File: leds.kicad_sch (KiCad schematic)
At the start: 20 parts

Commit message: Updated layout and schem
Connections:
- net 12v_PWD_LED_VOL_DIV: now reaches R6.1, R7.1, R8.1
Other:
- moved on the sheet: R7
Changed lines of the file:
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@@
+	)
+	(junction
+		(at 208.28 41.91)
+		(diameter 0)
+		(color 0 0 0 0)
 	)
 	(junction
@@
 	(wire
 		(pts
+			(xy 208.28 41.91) (xy 212.09 41.91)
+		)
+		(stroke
+			(width 0)
+			(type default)
+		)
+	)
+	(wire
+		(pts
 			(xy 173.99 38.1) (xy 181.61 38.1)
 		)
@@
 	(wire
 		(pts
-			(xy 208.28 41.91) (xy 208.28 38.1)
+			(xy 208.28 43.18) (xy 208.28 41.91)
 		)
 		(stroke
@@
 	(wire
 		(pts
-			(xy 208.28 49.53) (xy 208.28 50.8)
+			(xy 208.28 50.8) (xy 208.28 53.34)
 		)
 		(stroke
@@
 		(pts
 			(xy 129.54 35.56) (xy 129.54 46.99)
+		)
+		(stroke
+			(width 0)
+			(type default)
+		)
+	)
+	(wire
+		(pts
+			(xy 208.28 38.1) (xy 208.28 41.91)
 		)
 		(stroke
@@
 	(label "PUMP_PWM_IND_LED_5v"
 		(at 52.07 66.04 0)
+		(fields_autoplaced yes)
+		(effects
+			(font
+				(size 1.27 1.27)
+			)
+			(justify left bottom)
+		)
+	)
+	(label "12v_PWD_LED_VOL_DIV"
+		(at 212.09 41.91 0)
 		(fields_autoplaced yes)
 		(effects
@@
 	(symbol
 		(lib_id "Device:R")
-		(at 208.28 45.72 0)
+		(at 208.28 46.99 0)
 		(unit 1)
 		(exclude_from_sim no)
@@
 		(fields_autoplaced yes)
 		(property "Reference" "R7"
-			(at 210.82 44.4499 0)
+			(at 210.82 45.7199 0)
 			(effects
 				(font
@@
 		)
 		(property "Value" "470R"
-			(at 210.82 46.9899 0)
+			(at 210.82 48.2599 0)
 			(effects
 				(font
@@
 		)
 		(property "Footprint" "Resistor_SMD:R_0805_2012Metric"
-			(at 206.502 45.72 90)
+			(at 206.502 46.99 90)
 			(effects
 				(font
@@
 		)
 		(property "Datasheet" "~"
-			(at 208.28 45.72 0)
+			(at 208.28 46.99 0)
 			(effects
 				(font
@@
 		)
 		(property "Description" "Resistor"
-			(at 208.28 45.72 0)
+			(at 208.28 46.99 0)
 			(effects
 				(font
@@
 	(symbol
 		(lib_id "power:GND")
-		(at 208.28 50.8 0)
+		(at 208.28 53.34 0)
 		(unit 1)
 		(exclude_from_sim no)
@@
 		(fields_autoplaced yes)
 		(property "Reference" "#PWR049"
-			(at 208.28 57.15 0)
+			(at 208.28 59.69 0)
 			(effects
 				(font
@@
 		)
 		(property "Value" "GND"
-			(at 208.28 55.88 0)
+			(at 208.28 58.42 0)
 			(effects
 				(font
@@
 		)
 		(property "Footprint" ""
-			(at 208.28 50.8 0)
+			(at 208.28 53.34 0)
 			(effects
 				(font
@@
 		)
 		(property "Datasheet" ""
-			(at 208.28 50.8 0)
+			(at 208.28 53.34 0)
 			(effects
 				(font
@@
 		)
 		(property "Description" "Power symbol creates a global label with name \"GND\" , ground"
-			(at 208.28 50.8 0)
-			(effects
-				(font
+			(at 208.28 53.34 0)
+			(effects
+				(font

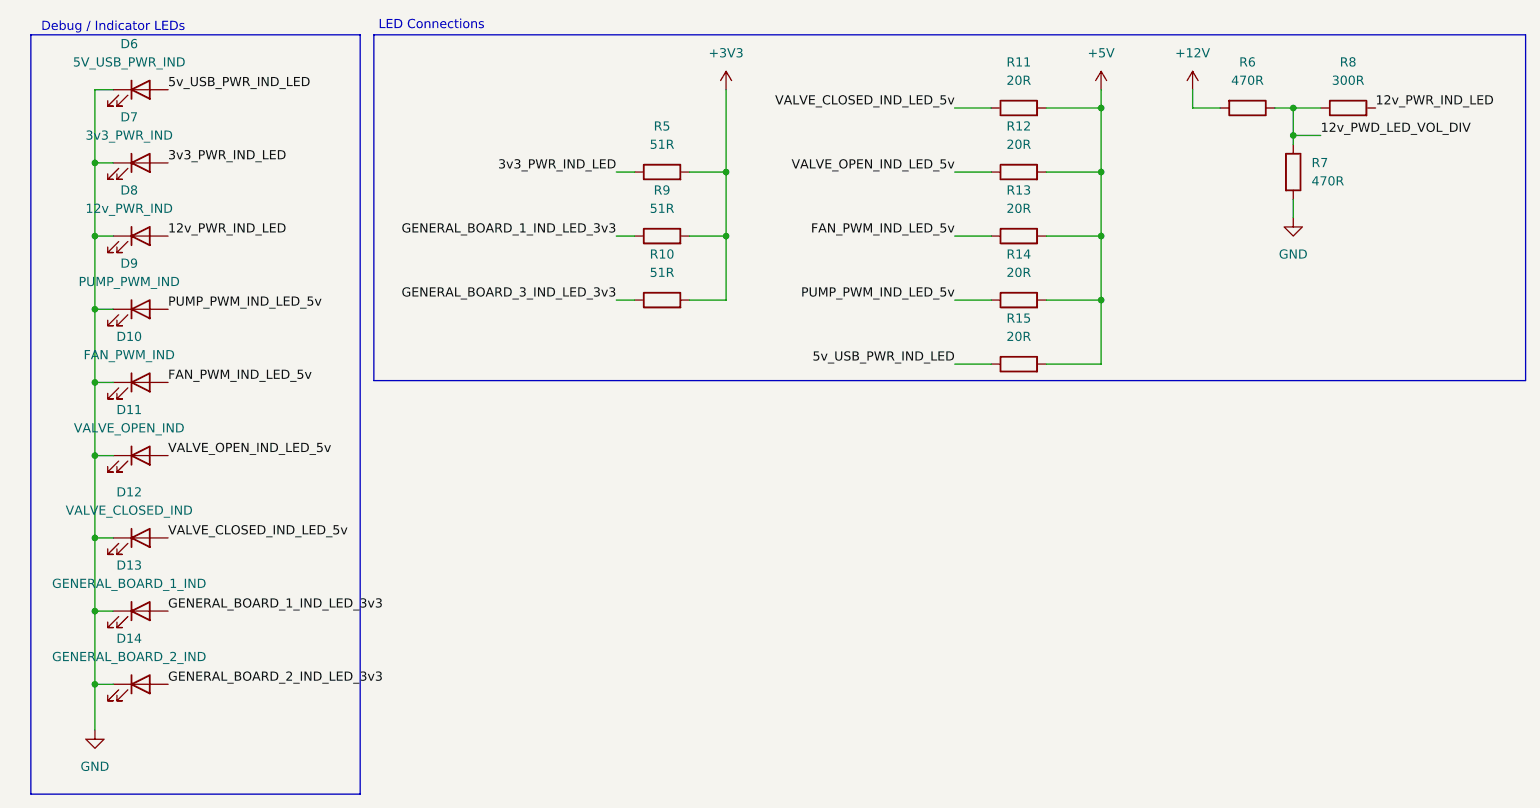
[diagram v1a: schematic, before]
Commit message: Layout of indicator LEDs. Shrank design space
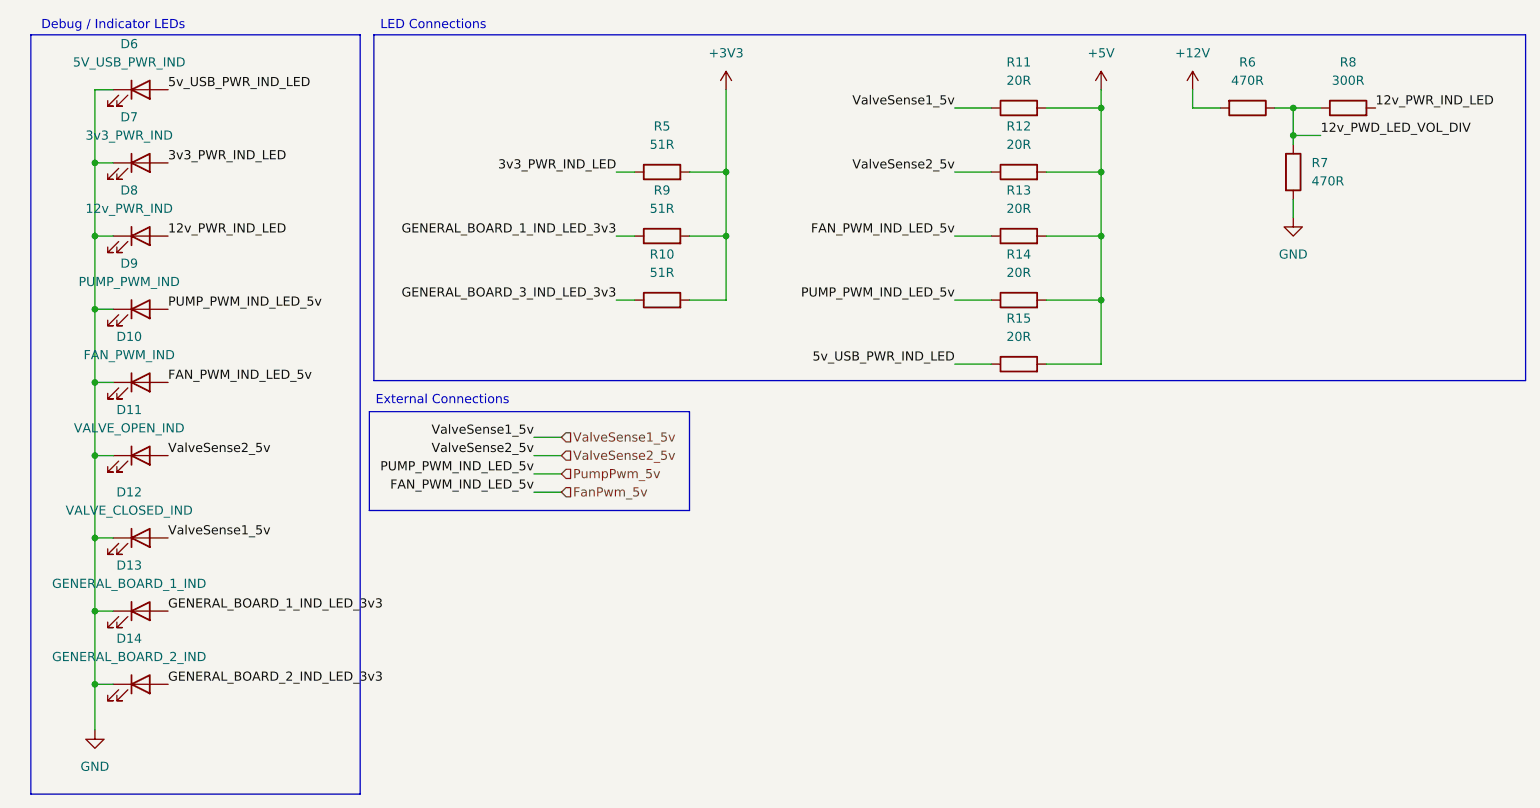
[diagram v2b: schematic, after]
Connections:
- net FAN_PWM_IND_LED_5v renamed FanPwm_5v
- net PUMP_PWM_IND_LED_5v renamed PumpPwm_5v
- net VALVE_CLOSED_IND_LED_5v renamed ValveSense1_5v
- net VALVE_OPEN_IND_LED_5v renamed ValveSense2_5v
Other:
- note added: "External Connections"
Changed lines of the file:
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@@
+	(wire
+		(pts
+			(xy 102.87 86.36) (xy 106.68 86.36)
+		)
+		(stroke
+			(width 0)
+			(type default)
+		)
+	)
 	(wire
 		(pts
@@
 	(wire
 		(pts
+			(xy 102.87 83.82) (xy 106.68 83.82)
+		)
+		(stroke
+			(width 0)
+			(type default)
+		)
+	)
+	(wire
+		(pts
 			(xy 114.3 55.88) (xy 116.84 55.88)
 		)
@@
 	(wire
 		(pts
+			(xy 102.87 91.44) (xy 106.68 91.44)
+		)
+		(stroke
+			(width 0)
+			(type default)
+		)
+	)
+	(wire
+		(pts
 			(xy 129.54 46.99) (xy 124.46 46.99)
 		)
@@
 		(pts
 			(xy 41.91 118.11) (xy 41.91 107.95)
+		)
+		(stroke
+			(width 0)
+			(type default)
+		)
+	)
+	(wire
+		(pts
+			(xy 102.87 88.9) (xy 106.68 88.9)
 		)
 		(stroke
@@
 		)
 	)
+	(rectangle
+		(start 80.01 80.264)
+		(end 124.46 93.98)
+		(stroke
+			(width 0)
+			(type default)
+		)
+		(fill
+			(type none)
+		)
+	)
 	(text "Debug / Indicator LEDs"
 		(exclude_from_sim no)
-		(at 44.45 26.924 0)
+		(at 44.45 26.67 0)
+		(effects
+			(font
+				(size 1.27 1.27)
+			)
+		)
+	)
+	(text "External Connections"
+		(exclude_from_sim no)
+		(at 90.17 78.74 0)
 		(effects
 			(font
@@
 	(text "LED Connections"
 		(exclude_from_sim no)
-		(at 88.646 26.67 0)
+		(at 88.9 26.67 0)
 		(effects
 			(font
@@
 		)
 	)
+	(label "ValveSense2_5v"
+		(at 52.07 86.36 0)
+		(fields_autoplaced yes)
+		(effects
+			(font
+				(size 1.27 1.27)
+			)
+			(justify left bottom)
+		)
+	)
+	(label "FAN_PWM_IND_LED_5v"
+		(at 102.87 91.44 180)
+		(fields_autoplaced yes)
+		(effects
+			(font
+				(size 1.27 1.27)
+			)
+			(justify right bottom)
+		)
+	)
 	(label "FAN_PWM_IND_LED_5v"
 		(at 52.07 76.2 0)
@@
 		)
 	)
+	(label "PUMP_PWM_IND_LED_5v"
+		(at 102.87 88.9 180)
+		(fields_autoplaced yes)
+		(effects
+			(font
+				(size 1.27 1.27)
+			)
+			(justify right bottom)
+		)
+	)
 	(label "5v_USB_PWR_IND_LED"
 		(at 52.07 35.56 0)
@@
 		)
 	)
+	(label "ValveSense1_5v"
+		(at 102.87 83.82 180)
+		(fields_autoplaced yes)
+		(effects
+			(font
+				(size 1.27 1.27)
+			)
+			(justify right bottom)
+		)
+	)
 	(label "GENERAL_BOARD_1_IND_LED_3v3"
 		(at 114.3 55.88 180)
@@
 		)
 	)
+	(label "ValveSense1_5v"
+		(at 52.07 97.79 0)
+		(fields_autoplaced yes)
+		(effects
+			(font
+				(size 1.27 1.27)
+			)
+			(justify left bottom)
+		)
+	)
 	(label "3v3_PWR_IND_LED"
 		(at 52.07 45.72 0)
@@
 		)
 	)
-	(label "VALVE_CLOSED_IND_LED_5v"
-		(at 52.07 97.79 0)
-		(fields_autoplaced yes)
-		(effects
-			(font
-				(size 1.27 1.27)
-			)
-			(justify left bottom)
-		)
-	)
-	(label "VALVE_OPEN_IND_LED_5v"
+	(label "ValveSense2_5v"
 		(at 161.29 46.99 180)
 		(fields_autoplaced yes)
@@
 		)
 	)
+	(label "ValveSense2_5v"
+		(at 102.87 86.36 180)
+		(fields_autoplaced yes)
+		(effects
+			(font
+				(size 1.27 1.27)
+			)
+			(justify right bottom)
+		)
+	)
+	(label "ValveSense1_5v"
+		(at 161.29 38.1 180)
+		(fields_autoplaced yes)
+		(effects
+			(font
+				(size 1.27 1.27)
+			)
+			(justify right bottom)
+		)
+	)
 	(label "GENERAL_BOARD_3_IND_LED_3v3"
 		(at 114.3 64.77 180)
@@
 		)
 	)
-	(label "VALVE_CLOSED_IND_LED_5v"
-		(at 161.29 38.1 180)
-		(fields_autoplaced yes)
-		(effects
-			(font
-				(size 1.27 1.27)
-			)
-			(justify right bottom)
-		)
-	)
-	(label "VALVE_OPEN_IND_LED_5v"
-		(at 52.07 86.36 0)
-		(fields_autoplaced yes)
-		(effects
-			(font
-				(size 1.27 1.27)
-			)
-			(justify left bottom)
-		)
-	)
+	(hierarchical_label "ValveSense2_5v"
+		(shape input)
+		(at 106.68 86.36 0)
+		(fields_autoplaced yes)
+		(effects
+			(font
+				(size 1.27 1.27)
+			)
+			(justify left)
+		)
+	)
+	(hierarchical_label "PumpPwm_5v"
+		(shape input)
+		(at 106.68 88.9 0)
+		(fields_autoplaced yes)
+		(effects
+			(font
+				(size 1.27 1.27)
+			)
+			(justify left)
+		)
+	)
+	(hierarchical_label "FanPwm_5v"
+		(shape input)
+		(at 106.68 91.44 0)
+		(fields_autoplaced yes)
+		(effects
+			(font
+				(size 1.27 1.27)
+			)
+			(justify left)
+		)
+	)
+	(hierarchical_label "ValveSense1_5v"
+		(shape input)
+		(at 106.68 83.82 0)
+		(fields_autoplaced yes)
+		(effects
+			(font
+				(size 1.27 1.27)
+			)
+			(justify left)
+		)
+	)

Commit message: Initial Layout
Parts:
- removed D13: GENERAL_BOARD_1_IND, LED_SMD:LED_0603_1608Metric, symbol Device:LED
- removed D14: GENERAL_BOARD_2_IND, LED_SMD:LED_0603_1608Metric, symbol Device:LED
- removed R10, R9: 51R, Resistor_SMD:R_0805_2012Metric, symbol Device:R

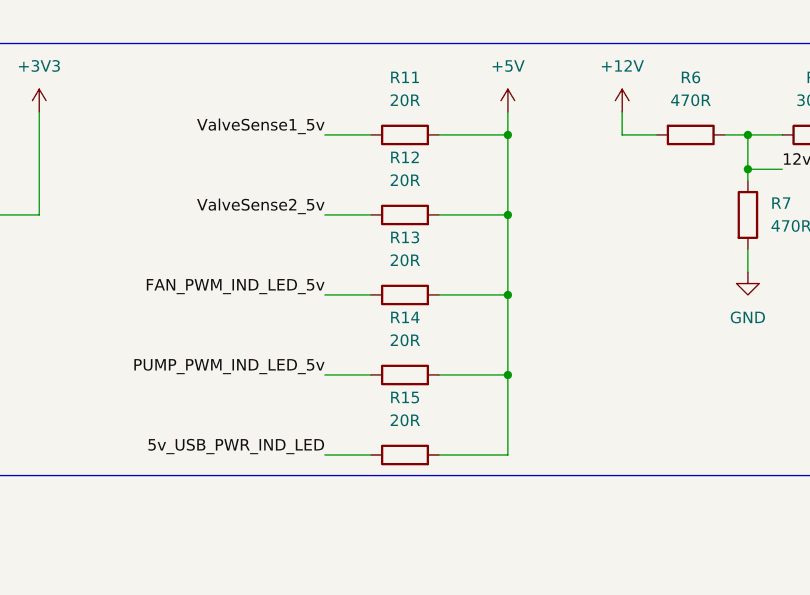
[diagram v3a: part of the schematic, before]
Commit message: Added all part numbers
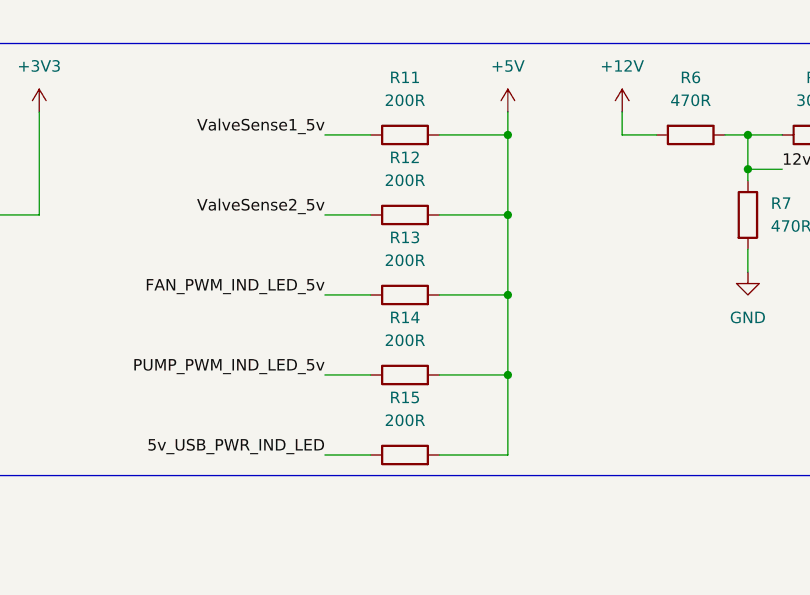
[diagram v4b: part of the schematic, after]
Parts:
- D10, D9: LCSC (none) -> C2297
- D11, D12: LCSC (none) -> C2296
- D6, D7, D8: LCSC (none) -> C2286
- R11, R12, R13, R14, R15: value 20R -> 200R; LCSC (none) -> C17540
- R5, R6, R7: LCSC (none) -> C17738
- R8: footprint Resistor_SMD:R_1206_3216Metric -> Resistor_SMD:R_0805_2012Metric; LCSC (none) -> C17617
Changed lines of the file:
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@@
 			)
 		)
-		(property "Value" "20R"
+		(property "Value" "200R"
 			(at 170.18 52.07 90)
 			(effects
@@
 		)
 		(property "URL" "https://jlcpcb.com/partdetail/18426-0805W8F510JT5E/C17738"
+			(at 170.18 55.88 0)
+			(effects
+				(font
+					(size 1.27 1.27)
+				)
+				(hide yes)
+			)
+		)
+		(property "LCSC" "C17540"
 			(at 170.18 55.88 0)
 			(effects
@@
 			)
 		)
-		(property "Value" "20R"
+		(property "Value" "200R"
 			(at 170.18 34.29 90)
 			(effects
@@
 		)
 		(property "URL" "https://jlcpcb.com/partdetail/18426-0805W8F510JT5E/C17738"
+			(at 170.18 38.1 0)
+			(effects
+				(font
+					(size 1.27 1.27)
+				)
+				(hide yes)
+			)
+		)
+		(property "LCSC" "C17540"
 			(at 170.18 38.1 0)
 			(effects
@@
 			)
 		)
+		(property "LCSC" "C2286"
+			(at 48.26 45.72 0)
+			(effects
+				(font
+					(size 1.27 1.27)
+				)
+				(hide yes)
+			)
+		)
 		(pin "1"
 		)
@@
 			)
 		)
+		(property "LCSC" "C2286"
+			(at 48.26 35.56 0)
+			(effects
+				(font
+					(size 1.27 1.27)
+				)
+				(hide yes)
+			)
+		)
 		(pin "1"
 		)
@@
 			)
 		)
+		(property "LCSC" "C2286"
+			(at 48.26 55.88 0)
+			(effects
+				(font
+					(size 1.27 1.27)
+				)
+				(hide yes)
+			)
+		)
 		(pin "1"
 		)
@@
 			)
 		)
-		(property "Value" "20R"
+		(property "Value" "200R"
 			(at 170.18 60.96 90)
 			(effects
@@
 			)
 		)
+		(property "LCSC" "C17540"
+			(at 170.18 64.77 0)
+			(effects
+				(font
+					(size 1.27 1.27)
+				)
+				(hide yes)
+			)
+		)
 		(pin "2"
 		)
@@
 			)
 		)
+		(property "LCSC" "C2296"
+			(at 48.26 86.36 0)
+			(effects
+				(font
+					(size 1.27 1.27)
+				)
+				(hide yes)
+			)
+		)
 		(pin "1"
 		)
@@
 		)
 		(property "Description" "Light emitting diode"
+			(at 48.26 97.79 0)
+			(effects
+				(font
+					(size 1.27 1.27)
+				)
+				(hide yes)
+			)
+		)
+		(property "LCSC" "C2296"
 			(at 48.26 97.79 0)
 			(effects
@@
 			)
 		)
+		(property "LCSC" "C17738"
+			(at 201.93 38.1 0)
+			(effects
+				(font
+					(size 1.27 1.27)
+				)
+				(hide yes)
+			)
+		)
 		(pin "2"
 		)
@@
 			)
 		)
-		(property "Footprint" "Resistor_SMD:R_1206_3216Metric"
+		(property "Footprint" "Resistor_SMD:R_0805_2012Metric"
 			(at 215.9 39.878 90)
 			(effects
@@
 		)
 		(property "MFR.Part #" "1206W4F3000T5E"
+			(at 215.9 38.1 0)
+			(effects
+				(font
+					(size 1.27 1.27)
+				)
+				(hide yes)
+			)
+		)
+		(property "LCSC" "C17617"
 			(at 215.9 38.1 0)
 			(effects
@@
 			)
 		)
+		(property "LCSC" "C17738"
+			(at 208.28 46.99 0)
+			(effects
+				(font
+					(size 1.27 1.27)
+				)
+				(hide yes)
+			)
+		)
 		(pin "2"
 		)
@@
 			)
 		)
-		(property "Value" "20R"
+		(property "Value" "200R"
 			(at 170.18 43.18 90)
 			(effects
@@
 		)
 		(property "URL" "https://jlcpcb.com/partdetail/18426-0805W8F510JT5E/C17738"
+			(at 170.18 46.99 0)
+			(effects
+				(font
+					(size 1.27 1.27)
+				)
+				(hide yes)
+			)
+		)
+		(property "LCSC" "C17540"
 			(at 170.18 46.99 0)
 			(effects
@@
 			)
 		)
+		(property "LCSC" "C17738"
+			(at 120.65 46.99 0)
+			(effects
+				(font
+					(size 1.27 1.27)
+				)
+				(hide yes)
+			)
+		)
 		(pin "2"
 		)
@@
 			)
 		)
+		(property "LCSC" "C2297"
+			(at 48.26 76.2 0)
+			(effects
+				(font
+					(size 1.27 1.27)
+				)
+				(hide yes)
+			)
+		)
 		(pin "1"
 		)
@@
 		)
 		(property "Description" "Light emitting diode"
+			(at 48.26 66.04 0)
+			(effects
+				(font
+					(size 1.27 1.27)
+				)
+				(hide yes)
+			)
+		)
+		(property "LCSC" "C2297"
 			(at 48.26 66.04 0)
 			(effects
@@
 			)
 		)
-		(property "Value" "20R"
+		(property "Value" "200R"
 			(at 170.18 69.85 90)
 			(effects
@@
 			(at 170.18 73.66 0)
 			(effects
+				(font
+					(size 1.27 1.27)
+				)
+				(hide yes)
+			)
+		)
+		(property "LCSC" "C17540"
+			(at 170.18 73.66 0)
+			(effects
